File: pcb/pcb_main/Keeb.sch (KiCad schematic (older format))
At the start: 39 parts, among them J1 TRRS_SJ1-42514, SW1 SW_RST, U1 ATMEGA32U4, U2 SN74HC138D‎, U3 SN74HC251, X1 XTAL_GND

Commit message: First pass at split pcb design completed
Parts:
- added ColL0, ColL1, ColL2, ColL3, ColL4, ColL5, ColL6, ColL7, ColR0, ColR1, ColR2, ColR3, ColR4, ColR5, ColR6, ColR7, Row0, Row1, Row2, Row3, Row4, Row5, Row6, Row7: Conn_01x01_Male, SVastaCustomParts:Mill-Max_Pin_Socket_7305-0-15-15-47-27-10-0, symbol Connector:Conn_01x01_Male
- SW1: symbol Keyboard_Parts:SW_PUSH -> Keeb-rescue:SW_PUSH-Keyboard_Parts-Keeb-rescue
- U1: symbol Keyboard_Parts:ATMEGA32U4 -> Keeb-rescue:ATMEGA32U4-Keyboard_Parts-Keeb-rescue
- X1: symbol Keyboard_Parts:XTAL_GND -> Keeb-rescue:XTAL_GND-Keyboard_Parts-Keeb-rescue
- renumbered D507 to D500, D506 to D501, D505 to D502, D504 to D503, D503 to D504, D502 to D505, D501 to D506, D500 to D507
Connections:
- net labels added: Col0, Col1, Col2, Col3, Col4, Col5, Col6, Col7, Row0, Row1, Row2, Row3, Row4, Row5, Row6, Row7
- wire segments 230 -> 269
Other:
- moved on the sheet: D500, D501, D502, D503, D504, D506, D507, R20, U2, U3

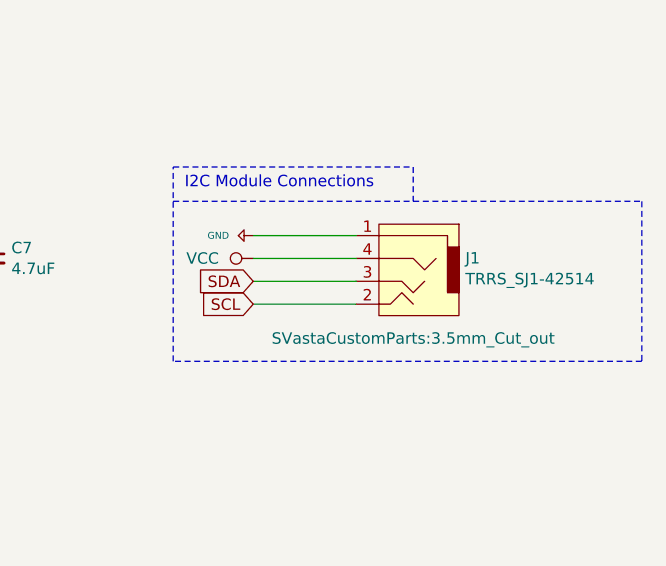
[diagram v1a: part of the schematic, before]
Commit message: Rev 1 of module 2 & updated all-in-one cad drawing
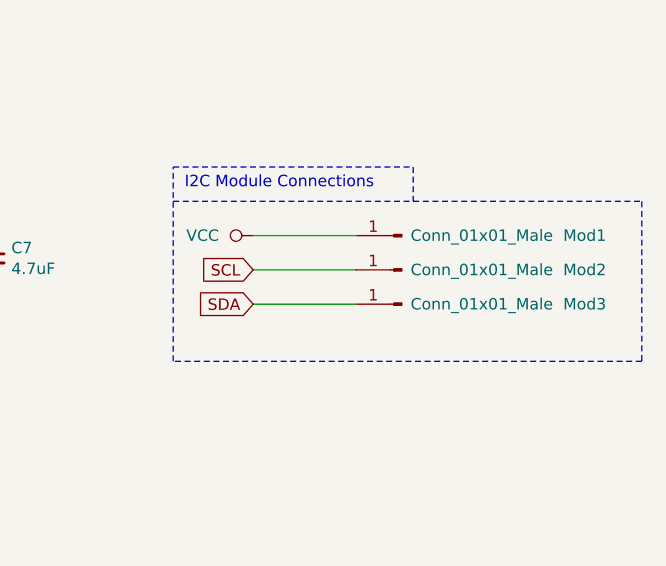
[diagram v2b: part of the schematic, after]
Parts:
- removed J1: TRRS_SJ1-42514, SVastaCustomParts:3.5mm_Cut_out, symbol SVastaCustomParts:TRRS_SJ1-42514
- added Mod1, Mod2, Mod3: Conn_01x01_Male, SVastaCustomParts:Mill-Max_Pin_Socket_7305-0-15-15-47-27-10-0, symbol Connector:Conn_01x01_Male
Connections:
- net SCL: now also Mod2.1 (Pin_1)
- net SDA: now also Mod3.1 (Pin_1)
- net VCC: now also Mod1.1 (Pin_1)
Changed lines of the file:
@@
 Wire Wire Line
 	6700 4350 6850 4350
-Text GLabel 9350 1750 0    50   Input ~ 0
+Text GLabel 9350 1600 0    50   Input ~ 0
 SCL
 Text GLabel 3800 4150 0    50   Input ~ 0
@@
 Wire Wire Line
 	3950 4750 3800 4750
-$Comp
-L SVastaCustomParts:TRRS_SJ1-42514 J1
-U 1 1 5D8C84D5
-P 10050 1300
-F 0 "J1" H 9822 1051 50  0000 R CNN
-F 1 "TRRS_SJ1-42514" H 9822 960 50  0000 R CNN
-F 2 "SVastaCustomParts:3.5mm_Cut_out" H 10050 700 50  0000 C CNN
-F 3 "https://www.cui.com/product/resource/sj1-4251x-series.pdf" H 10050 1300 50  0001 C CNN
-	1    10050 1300
-	-1   0    0    -1
-$EndComp
 $Comp
 L SVastaCustomParts:CD74AC138E U2
@@
 Wire Wire Line
 	5550 1150 5350 1150
-$Comp
-L Keeb-rescue:GND-Keyboard_Parts-Keeb-rescue #PWR0130
-U 1 1 5E039B9B
-P 9350 1450
-F 0 "#PWR0130" H 9350 1500 20  0001 C CNN
-F 1 "GND" V 9350 1250 30  0000 L CNN
-F 2 "" H 9350 1450 60  0000 C CNN
-F 3 "" H 9350 1450 60  0000 C CNN
-	1    9350 1450
-	0    1    1    0
-$EndComp
 Text GLabel 4150 3050 0    50   BiDi ~ 0
 SS1
@@
 L power:VCC #PWR0129
 U 1 1 5E03963C
-P 9350 1550
-F 0 "#PWR0129" H 9350 1400 50  0001 C CNN
-F 1 "VCC" V 9350 1700 50  0000 L CNN
-F 2 "" H 9350 1550 50  0001 C CNN
-F 3 "" H 9350 1550 50  0001 C CNN
-	1    9350 1550
-	0    -1   -1   0
-$EndComp
-Text GLabel 9350 1650 0    50   Input ~ 0
+P 9350 1450
+F 0 "#PWR0129" H 9350 1300 50  0001 C CNN
+F 1 "VCC" V 9350 1600 50  0000 L CNN
+F 2 "" H 9350 1450 50  0001 C CNN
+F 3 "" H 9350 1450 50  0001 C CNN
+	1    9350 1450
+	0    -1   -1   0
+$EndComp
+Text GLabel 9350 1750 0    50   Input ~ 0
 SDA
 Text Label 9950 5100 2    50   ~ 0
@@
 	9350 1450 9800 1450
 Wire Wire Line
-	9350 1550 9800 1550
-Wire Wire Line
-	9350 1650 9800 1650
+	9350 1600 9800 1600
 Wire Wire Line
 	9350 1750 9800 1750
@@
 Text Label 2450 6000 0    50   ~ 0
 Row7
+$Comp
+L Connector:Conn_01x01_Male Mod1
+U 1 1 5E9653F7
+P 10000 1450
+F 0 "Mod1" H 9200 1450 50  0000 C CNN
+F 1 "Conn_01x01_Male" H 9650 1450 50  0000 C CNN
+F 2 "SVastaCustomParts:Mill-Max_Pin_Socket_7305-0-15-15-47-27-10-0" H 10000 1450 50  0001 C CNN
+F 3 "~" H 10000 1450 50  0001 C CNN
+	1    10000 1450
+	-1   0    0    1
+$EndComp
+$Comp
+L Connector:Conn_01x01_Male Mod2
+U 1 1 5E97AB3B
+P 10000 1600
+F 0 "Mod2" H 9200 1600 50  0000 C CNN
+F 1 "Conn_01x01_Male" H 9650 1600 50  0000 C CNN
+F 2 "SVastaCustomParts:Mill-Max_Pin_Socket_7305-0-15-15-47-27-10-0" H 10000 1600 50  0001 C CNN
+F 3 "~" H 10000 1600 50  0001 C CNN
+	1    10000 1600
+	-1   0    0    1
+$EndComp
+$Comp
+L Connector:Conn_01x01_Male Mod3
+U 1 1 5E98FEDE
+P 10000 1750
+F 0 "Mod3" H 9200 1750 50  0000 C CNN
+F 1 "Conn_01x01_Male" H 9650 1750 50  0000 C CNN
+F 2 "SVastaCustomParts:Mill-Max_Pin_Socket_7305-0-15-15-47-27-10-0" H 10000 1750 50  0001 C CNN
+F 3 "~" H 10000 1750 50  0001 C CNN
+	1    10000 1750
+	-1   0    0    1
+$EndComp
 $EndSCHEMATC

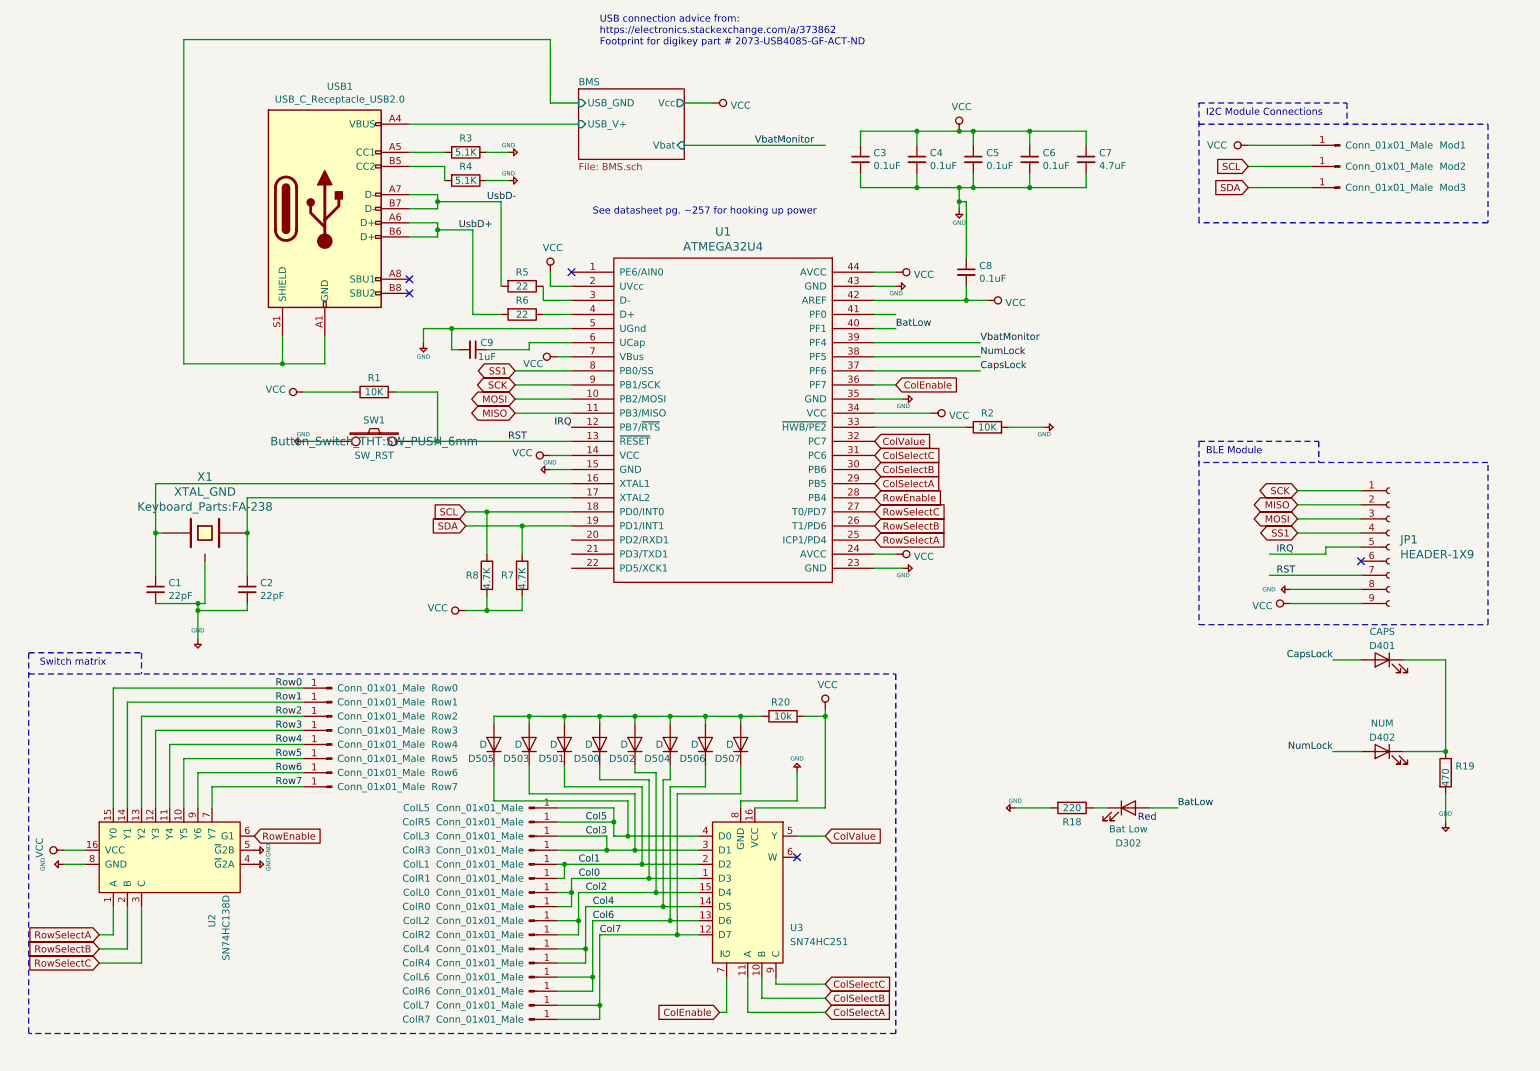
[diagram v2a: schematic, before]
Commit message: Updated connection method on main pcb
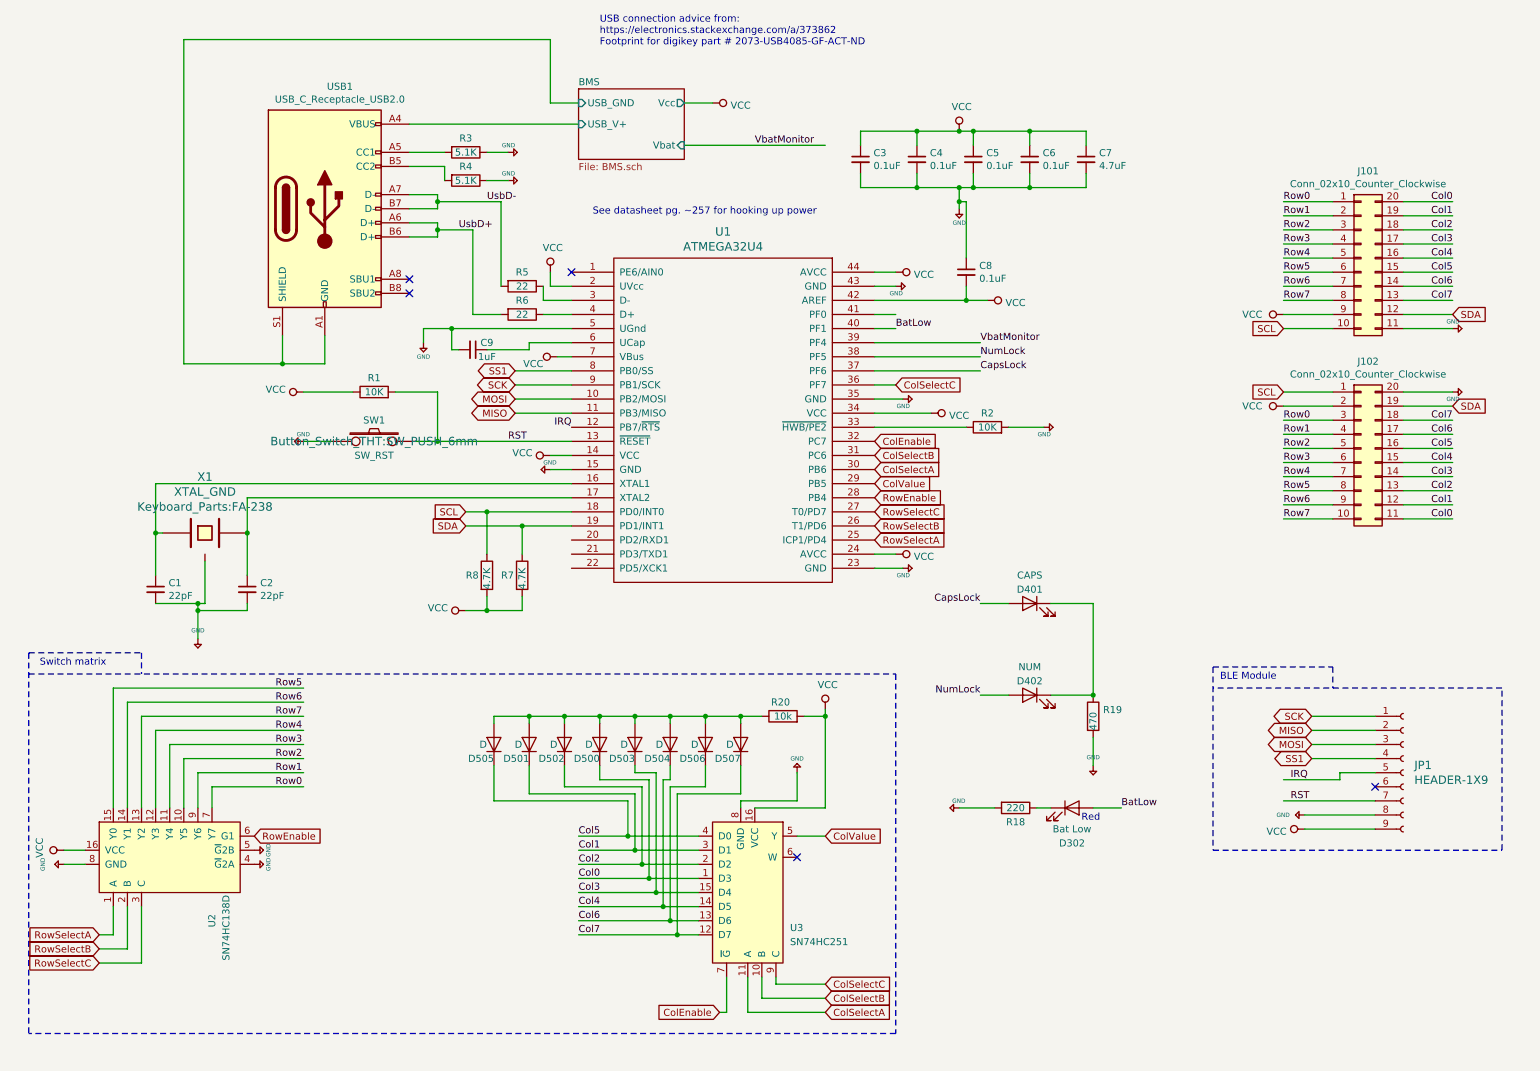
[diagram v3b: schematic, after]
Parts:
- removed ColL0, ColL1, ColL2, ColL3, ColL4, ColL5, ColL6, ColL7, ColR0, ColR1, ColR2, ColR3, ColR4, ColR5, ColR6, ColR7, Mod1, Mod2, Mod3, Row0, Row1, Row2, Row3, Row4, Row5, Row6, Row7: Conn_01x01_Male, SVastaCustomParts:Mill-Max_Pin_Socket_7305-0-15-15-47-27-10-0, symbol Connector:Conn_01x01_Male
- added J101, J102: Conn_02x10_Counter_Clockwise, SVastaCustomParts:Backplane_Connector_Hirose_PCN_20pos_Plug, symbol Connector_Generic:Conn_02x10_Counter_Clockwise
- D500, D504, D505, D506, D507: footprint SVastaCustomParts:D_MiniMELF_Handsoldering_Shorter_Pads -> Diode_SMD:D_0805_2012Metric_Pad1.15x1.40mm_HandSolder
- D501: renamed from D503; footprint SVastaCustomParts:D_MiniMELF_Handsoldering_Shorter_Pads -> Diode_SMD:D_0805_2012Metric_Pad1.15x1.40mm_HandSolder
- D502: renamed from D501; footprint SVastaCustomParts:D_MiniMELF_Handsoldering_Shorter_Pads -> Diode_SMD:D_0805_2012Metric_Pad1.15x1.40mm_HandSolder
- D503: renamed from D502; footprint SVastaCustomParts:D_MiniMELF_Handsoldering_Shorter_Pads -> Diode_SMD:D_0805_2012Metric_Pad1.15x1.40mm_HandSolder
- R20: footprint Resistor_THT:R_Axial_DIN0204_L3.6mm_D1.6mm_P5.08mm_Horizontal -> Resistor_SMD:R_0805_2012Metric_Pad1.15x1.40mm_HandSolder
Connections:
- wire segments 268 -> 275
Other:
- note removed: "I2C Module Connections"
- moved on the sheet: D302, D401, D402, JP1, R18, R19
